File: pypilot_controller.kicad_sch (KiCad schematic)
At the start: 39 parts, among them J1 power+, J10 Clutch, J2 power-, J3 Motor A, J4 Motor B, Q1 Q_NMOS_GDS, Q2 Q_NMOS_GDS, Q3 Q_NMOS_GDS, Q4 Q_NMOS_GDS, Q5 Q_NMOS_GDS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

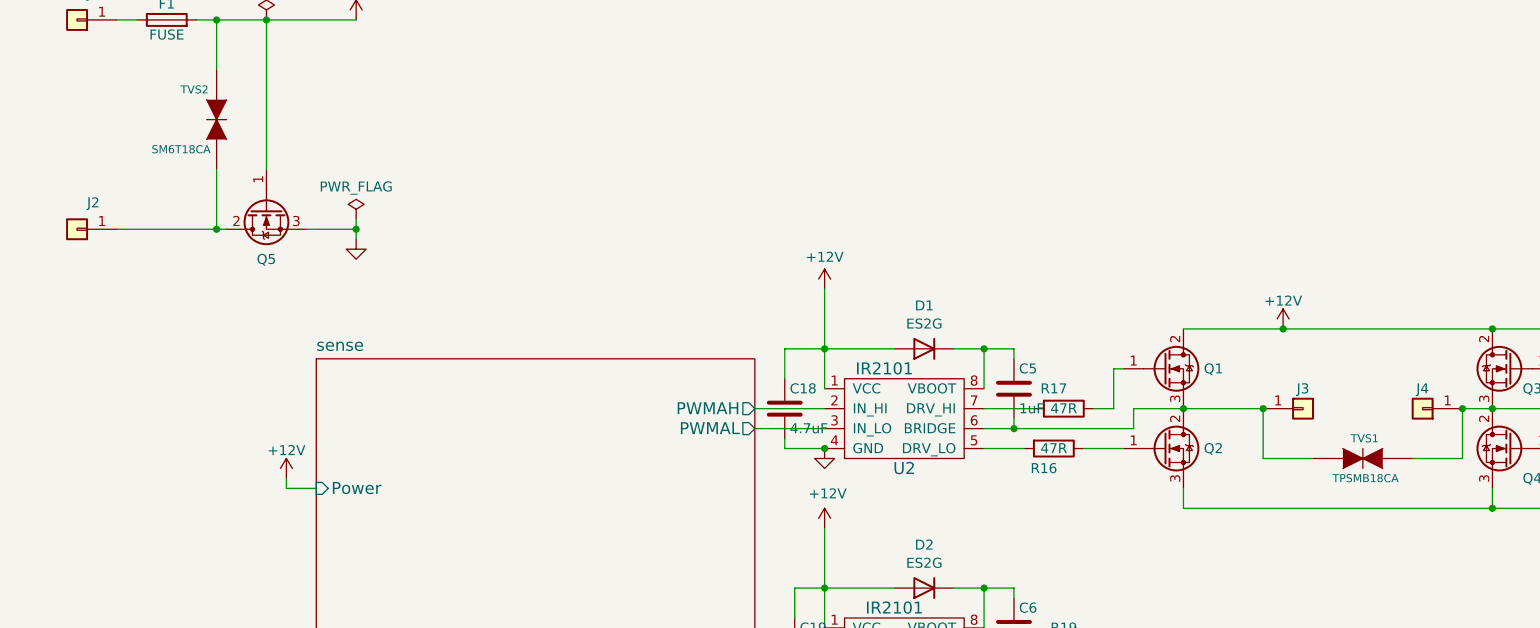
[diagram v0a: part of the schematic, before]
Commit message: Update TVS diodes to be cheapest of all the options Sean mentioned
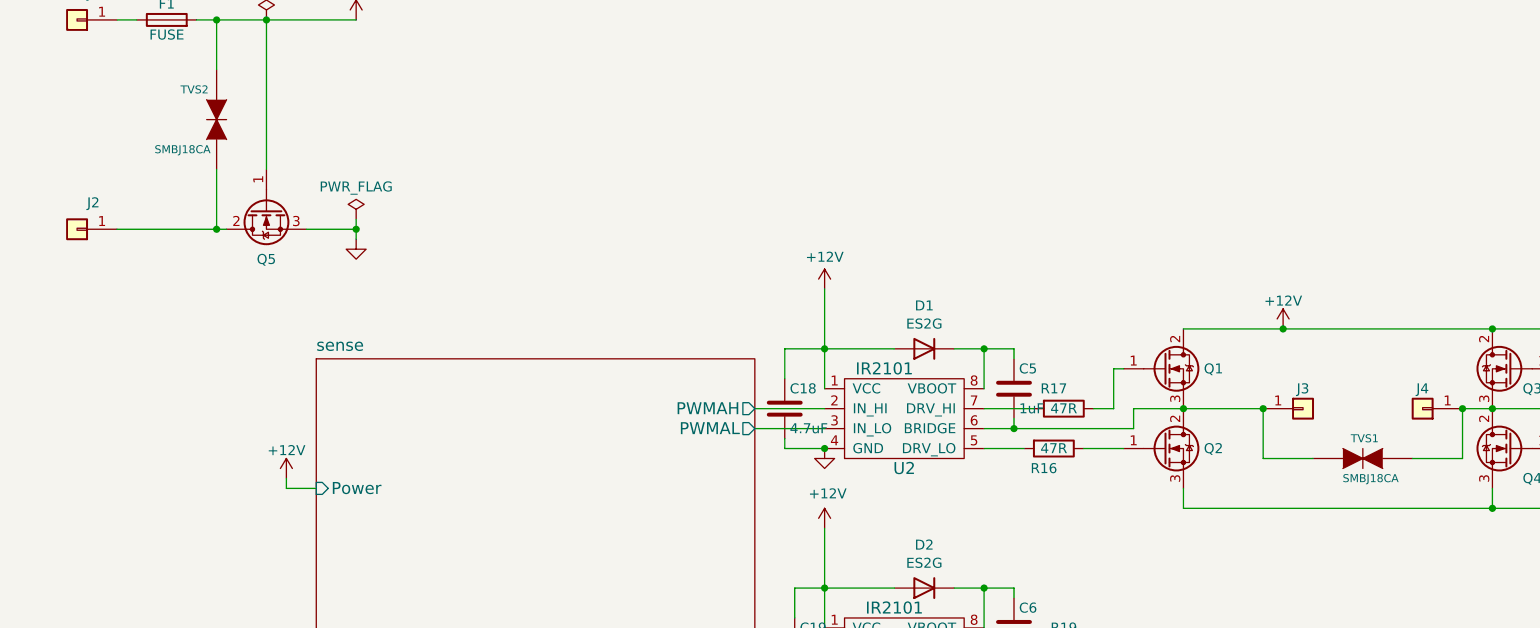
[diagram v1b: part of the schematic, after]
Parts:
- TVS1: value TPSMB18CA -> SMBJ18CA; LCSC *C83327, C468907 -> C83327
- TVS2: value SM6T18CA -> SMBJ18CA; LCSC *C83327, C283478 -> C83327
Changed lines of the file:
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@@
 			)
 		)
-		(property "Value" "TPSMB18CA"
+		(property "Value" "SMBJ18CA"
 			(at 201.422 88.9 0)
 			(effects
@@
 			)
 		)
-		(property "LCSC" "*C83327, C468907 "
+		(property "LCSC" "C83327"
 			(at 196.85 86.36 0)
 			(effects
@@
 			)
 		)
-		(property "Value" "SM6T18CA"
+		(property "Value" "SMBJ18CA"
 			(at 50.038 46.99 90)
 			(effects
@@
 			)
 		)
-		(property "LCSC" "*C83327, C283478"
+		(property "LCSC" "C83327"
 			(at 50.8 43.18 0)
 			(effects

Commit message: Updated screw terminals from C238164 to C481447, much cheaper
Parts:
- J1, J2, J3, J4: footprint pypilot_controller_footprints:screw_terminal -> lcsc:CONN-TH_T44001
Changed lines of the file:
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@@
 			)
 		)
-		(property "Footprint" "pypilot_controller_footprints:screw_terminal"
+		(property "Footprint" "lcsc:CONN-TH_T44001"
 			(at 33.02 57.15 0)
 			(effects
@@
 			)
 		)
-		(property "Footprint" "pypilot_controller_footprints:screw_terminal"
+		(property "Footprint" "lcsc:CONN-TH_T44001"
 			(at 33.02 30.48 0)
 			(effects
@@
 			)
 		)
-		(property "Footprint" "pypilot_controller_footprints:screw_terminal"
+		(property "Footprint" "lcsc:CONN-TH_T44001"
 			(at 189.23 80.01 0)
 			(effects
@@
 			)
 		)
-		(property "Footprint" "pypilot_controller_footprints:screw_terminal"
+		(property "Footprint" "lcsc:CONN-TH_T44001"
 			(at 204.47 80.01 0)
 			(effects

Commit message: Update 3d model and footprint for fuse holder
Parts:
- F1: footprint pypilot_controller_footprints:BladeFuse-CarType -> lcsc:FUSE-TH_BX503-35
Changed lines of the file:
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@@
 			)
 		)
-		(property "Footprint" "pypilot_controller_footprints:BladeFuse-CarType"
+		(property "Footprint" "lcsc:FUSE-TH_BX503-35"
 			(at 44.45 32.258 90)
 			(effects
@@
 			)
 		)
-		(property "Datasheet" "~"
+		(property "Datasheet" "https://www.lcsc.com/datasheet/lcsc_datasheet_2411201843_DEALON-BX503-35_C2935871.pdf"
 			(at 44.45 30.48 0)
 			(effects

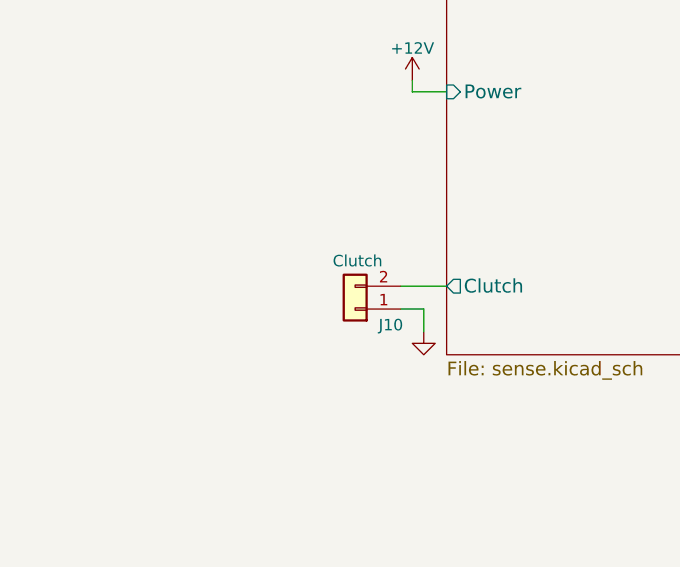
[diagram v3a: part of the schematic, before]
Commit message: Put clutch components onto separate sheet
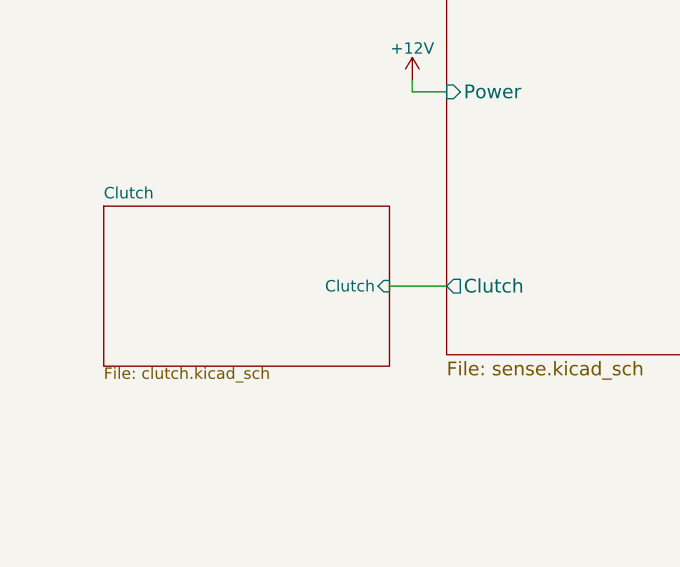
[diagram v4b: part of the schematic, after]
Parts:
- removed J10: Clutch, Connector_PinHeader_2.54mm:PinHeader_1x02_P2.54mm_Vertical, symbol Connector_Generic:Conn_01x02
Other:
- added sheet Clutch (clutch.kicad_sch)
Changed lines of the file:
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@@
 	(wire
 		(pts
-			(xy 58.42 114.3) (xy 60.96 114.3)
-		)
-		(stroke
-			(width 0)
-			(type default)
-		)
-	)
-	(wire
-		(pts
 			(xy 124.46 102.87) (xy 124.46 106.68)
 		)
@@
 	(wire
 		(pts
-			(xy 60.96 114.3) (xy 60.96 116.84)
-		)
-		(stroke
-			(width 0)
-			(type default)
-		)
-	)
-	(wire
-		(pts
 			(xy 165.1 80.01) (xy 165.1 74.93)
 		)
@@
 	(wire
 		(pts
+			(xy 57.15 111.76) (xy 63.5 111.76)
+		)
+		(stroke
+			(width 0)
+			(type default)
+		)
+	)
+	(wire
+		(pts
 			(xy 234.95 69.85) (xy 243.84 69.85)
 		)
@@
 	(wire
 		(pts
-			(xy 58.42 111.76) (xy 63.5 111.76)
-		)
-		(stroke
-			(width 0)
-			(type default)
-		)
-	)
-	(wire
-		(pts
 			(xy 128.27 85.09) (xy 123.19 85.09)
 		)
@@
 	)
 	(symbol
-		(lib_id "Connector_Generic:Conn_01x02")
-		(at 53.34 114.3 180)
-		(unit 1)
-		(exclude_from_sim no)
-		(in_bom yes)
-		(on_board yes)
-		(dnp no)
-		(property "Reference" "J10"
-			(at 58.674 116.078 0)
-			(effects
-				(font
-					(size 1.27 1.27)
-				)
-				(justify left)
-			)
-		)
-		(property "Value" "Clutch"
-			(at 56.388 108.966 0)
-			(effects
-				(font
-					(size 1.27 1.27)
-				)
-				(justify left)
-			)
-		)
-		(property "Footprint" "Connector_PinHeader_2.54mm:PinHeader_1x02_P2.54mm_Vertical"
-			(at 53.34 114.3 0)
-			(effects
-				(font
-					(size 1.27 1.27)
-				)
-				(hide yes)
-			)
-		)
-		(property "Datasheet" "~"
-			(at 53.34 114.3 0)
-			(effects
-				(font
-					(size 1.27 1.27)
-				)
-				(hide yes)
-			)
-		)
-		(property "Description" "Generic connector, single row, 01x02, script generated (kicad-library-utils/schlib/autogen/connector/)"
-			(at 53.34 114.3 0)
-			(effects
-				(font
-					(size 1.27 1.27)
-				)
-				(hide yes)
-			)
-		)
-		(pin "1"
-		)
-		(pin "2"
-		)
-		(instances
-			(project "pypilot_controller"
-				(path "/3485d22d-0932-4f13-a5db-09c3f9bc7038"
-					(reference "J10")
-					(unit 1)
-				)
-			)
-		)
-	)
-	(symbol
 		(lib_id "Mechanical:MountingHole")
 		(at 17.78 182.88 0)
@@
 	)
 	(symbol
-		(lib_id "power:GND")
-		(at 60.96 116.84 0)
-		(unit 1)
-		(exclude_from_sim no)
-		(in_bom yes)
-		(on_board yes)
-		(dnp no)
-		(property "Reference" "#PWR03"
-			(at 60.96 123.19 0)
-			(effects
-				(font
-					(size 1.27 1.27)
-				)
-				(hide yes)
-			)
-		)
-		(property "Value" "GND"
-			(at 57.15 118.11 0)
-			(effects
-				(font
-					(size 1.27 1.27)
-				)
-				(hide yes)
-			)
-		)
-		(property "Footprint" ""
-			(at 60.96 116.84 0)
-			(effects
-				(font
-					(size 1.27 1.27)
-				)
-				(hide yes)
-			)
-		)
-		(property "Datasheet" ""
-			(at 60.96 116.84 0)
-			(effects
-				(font
-					(size 1.27 1.27)
-				)
-				(hide yes)
-			)
-		)
-		(property "Description" "Power symbol creates a global label with name \"GND\" , ground"
-			(at 60.96 116.84 0)
-			(effects
-				(font
-					(size 1.27 1.27)
-				)
-				(hide yes)
-			)
-		)
-		(pin "1"
-		)
-		(instances
-			(project "pypilot_controller"
-				(path "/3485d22d-0932-4f13-a5db-09c3f9bc7038"
-					(reference "#PWR03")
-					(unit 1)
-				)
-			)
-		)
-	)
-	(symbol
 		(lib_id "power:PWR_FLAG")
 		(at 57.15 30.48 0)
@@
 				)
 			)
+		)
+	)
+	(sheet
+		(at 25.4 102.87)
+		(size 31.75 17.78)
+		(fields_autoplaced yes)
+		(stroke
+			(width 0.1524)
+			(type solid)
+			(color 132 0 132 1)
+		)
+		(fill
+			(color 255 255 255 0.0000)
+		)
+		(property "Sheetname" "Clutch"
+			(at 25.4 102.1584 0)
+			(effects
+				(font
+					(size 1.27 1.27)
+				)
+				(justify left bottom)
+			)
+		)
+		(property "Sheetfile" "clutch.kicad_sch"
+			(at 25.4 120.7266 0)
+			(effects
+				(font
+					(size 1.27 1.27)
+				)
+				(justify left top)
+			)
+		)
+		(pin "Clutch" input
+			(at 57.15 111.76 0)
+			(effects
+				(font
+					(size 1.27 1.27)
+				)
+				(justify right)
+			)
+		)
+		(instances
+			(project "pypilot_controller"
+				(path "/3485d22d-0932-4f13-a5db-09c3f9bc7038"
+					(page "4")
+				)
+			)

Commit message: Tweaks to hand-load components for current availability
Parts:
- J1, J2, J3, J4: LCSC C238164 -> C481447
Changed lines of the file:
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@@
 			)
 		)
-		(property "Datasheet" "~"
+		(property "Datasheet" "https://www.lcsc.com/datasheet/lcsc_datasheet_2304140030_BERYL-Electronic-Tech-RG063M331LO10-20TA-1A1E_C357629.pdf"
 			(at 229.87 80.01 0)
 			(effects
@@
 			)
 		)
-		(property "Datasheet" "~"
+		(property "Datasheet" "https://www.lcsc.com/datasheet/lcsc_datasheet_2304140030_BERYL-Electronic-Tech-RG063M331LO10-20TA-1A1E_C357629.pdf"
 			(at 234.95 86.36 0)
 			(effects
@@
 			)
 		)
-		(property "LCSC" "C238164"
+		(property "LCSC" "C481447"
 			(at 33.02 57.15 0)
 			(effects
@@
 			)
 		)
-		(property "LCSC" "C238164"
+		(property "LCSC" "C481447"
 			(at 33.02 30.48 0)
 			(effects
@@
 			)
 		)
-		(property "LCSC" "C238164"
+		(property "LCSC" "C481447"
 			(at 189.23 80.01 0)
 			(effects
@@
 			)
 		)
-		(property "LCSC" "C238164"
+		(property "LCSC" "C481447"
 			(at 204.47 80.01 0)
 			(effects

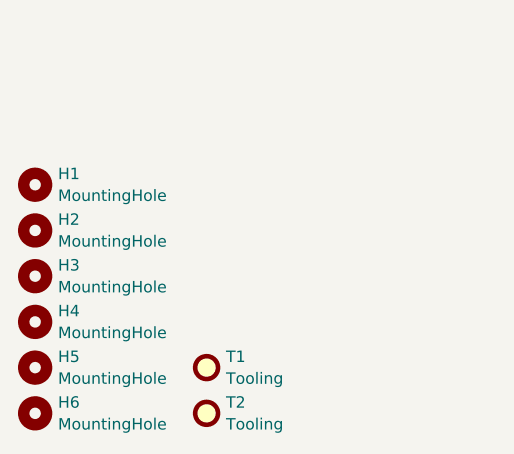
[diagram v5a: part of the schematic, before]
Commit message: Modify board outline to fit Daho 83X58X34 enclosure.  Remove mounting holes and move components.
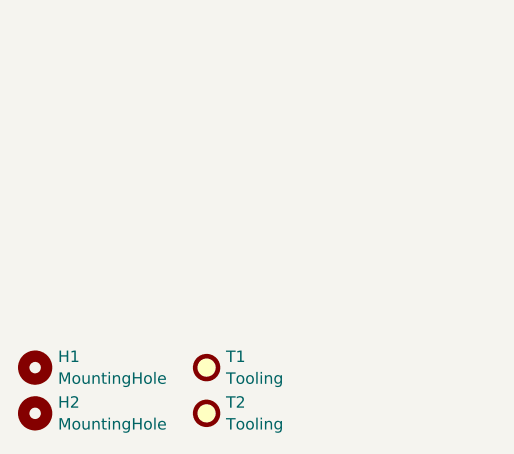
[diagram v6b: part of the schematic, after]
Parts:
- removed H1, H2, H3, H4: MountingHole, MountingHole:MountingHole_3.2mm_M3, symbol Mechanical:MountingHole
- renumbered H5 to H1, H6 to H2

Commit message: Added results of fit test to components received from LCSC
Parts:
- C10, C9: FitTest (none) -> ?
- D1, D2, J1, J2, J3, J4, Q1, Q2, Q3, Q4, Q5, R26, TVS1, TVS2, U2, U3: FitTest (none) -> Y
- F1: FitTest (none) -> N
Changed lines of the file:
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@@
+			)
+		)
+		(property "FitTest" "Y"
+			(at 215.9 85.09 0)
+			(effects
+				(font
+					(size 1.27 1.27)
+				)
+				(hide yes)
 			)
 		)
@@
 			)
 		)
+		(property "FitTest" "Y"
+			(at 138.43 73.66 0)
+			(effects
+				(font
+					(size 1.27 1.27)
+				)
+				(hide yes)
+			)
+		)
 		(pin "1"
 		)
@@
 		)
 		(property "LCSC" "C2956"
+			(at 138.43 104.14 0)
+			(effects
+				(font
+					(size 1.27 1.27)
+				)
+				(hide yes)
+			)
+		)
+		(property "FitTest" "Y"
 			(at 138.43 104.14 0)
 			(effects
@@
 			)
 		)
+		(property "FitTest" "Y"
+			(at 215.9 74.93 0)
+			(effects
+				(font
+					(size 1.27 1.27)
+				)
+				(hide yes)
+			)
+		)
 		(pin "2"
 		)
@@
 			)
 		)
+		(property "FitTest" "Y"
+			(at 171.45 74.93 0)
+			(effects
+				(font
+					(size 1.27 1.27)
+				)
+				(hide yes)
+			)
+		)
 		(pin "1"
 		)
@@
 			)
 		)
+		(property "FitTest" "Y"
+			(at 171.45 85.09 0)
+			(effects
+				(font
+					(size 1.27 1.27)
+				)
+				(hide yes)
+			)
+		)
 		(pin "2"
 		)
@@
 		)
 		(property "LCSC" "C83327"
+			(at 196.85 86.36 0)
+			(effects
+				(font
+					(size 1.27 1.27)
+				)
+				(hide yes)
+			)
+		)
+		(property "FitTest" "Y"
 			(at 196.85 86.36 0)
 			(effects
@@
 			)
 		)
+		(property "FitTest" "Y"
+			(at 57.15 54.61 0)
+			(effects
+				(font
+					(size 1.27 1.27)
+				)
+				(hide yes)
+			)
+		)
 		(pin "1"
 		)
@@
 			)
 		)
+		(property "FitTest" "?"
+			(at 229.87 80.01 0)
+			(effects
+				(font
+					(size 1.27 1.27)
+				)
+				(hide yes)
+			)
+		)
 		(pin "1"
 		)
@@
 			)
 		)
+		(property "FitTest" "?"
+			(at 234.95 86.36 0)
+			(effects
+				(font
+					(size 1.27 1.27)
+				)
+				(hide yes)
+			)
+		)
 		(pin "1"
 		)
@@
 			)
 		)
+		(property "FitTest" "Y"
+			(at 50.8 43.18 0)
+			(effects
+				(font
+					(size 1.27 1.27)
+				)
+				(hide yes)
+			)
+		)
 		(pin "1"
 		)
@@
 			)
 		)
+		(property "FitTest" "Y"
+			(at 140.97 72.39 0)
+			(effects
+				(font
+					(size 1.27 1.27)
+				)
+				(hide yes)
+			)
+		)
 		(pin "1"
 		)
@@
 			)
 		)
+		(property "FitTest" "Y"
+			(at 140.97 102.87 0)
+			(effects
+				(font
+					(size 1.27 1.27)
+				)
+				(hide yes)
+			)
+		)
 		(pin "1"
 		)
@@
 			)
 		)
+		(property "FitTest" "N"
+			(at 44.45 30.48 0)
+			(effects
+				(font
+					(size 1.27 1.27)
+				)
+				(hide yes)
+			)
+		)
 		(pin "1"
 		)
@@
 			)
 		)
+		(property "FitTest" "Y"
+			(at 33.02 57.15 0)
+			(effects
+				(font
+					(size 1.27 1.27)
+				)
+				(hide yes)
+			)
+		)
 		(pin "1"
 		)
@@
 			)
 		)
+		(property "FitTest" "Y"
+			(at 33.02 30.48 0)
+			(effects
+				(font
+					(size 1.27 1.27)
+				)
+				(hide yes)
+			)
+		)
 		(pin "1"
 		)
@@
 			)
 		)
+		(property "FitTest" "Y"
+			(at 189.23 80.01 0)
+			(effects
+				(font
+					(size 1.27 1.27)
+				)
+				(hide yes)
+			)
+		)
 		(pin "1"
 		)
@@
 		)
 		(property "LCSC" "C481447"
+			(at 204.47 80.01 0)
+			(effects
+				(font
+					(size 1.27 1.27)
+				)
+				(hide yes)
+			)
+		)
+		(property "FitTest" "Y"
 			(at 204.47 80.01 0)
 			(effects
@@
 			(effects
 				(font
+					(size 1.27 1.27)
+				)
+				(hide yes)
+			)
+		)
+		(property "FitTest" "Y"
+			(at 245.11 101.6 0)
+			(effects
+				(font

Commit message: Specify MOSFET
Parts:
- Q1, Q2, Q3, Q4, Q5: value Q_NMOS_GDS -> IRFR7440
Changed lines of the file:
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@@
 			)
 		)
-		(property "Value" "Q_NMOS_GDS"
+		(property "Value" "IRFR7440"
 			(at 209.5246 85.09 90)
 			(effects
@@
 			)
 		)
-		(property "Value" "Q_NMOS_GDS"
+		(property "Value" "IRFR7440"
 			(at 209.5246 74.93 90)
 			(effects
@@
 			)
 		)
-		(property "Value" "Q_NMOS_GDS"
+		(property "Value" "IRFR7440"
 			(at 177.8254 74.93 90)
 			(effects
@@
 			)
 		)
-		(property "Value" "Q_NMOS_GDS"
+		(property "Value" "IRFR7440"
 			(at 177.8254 85.09 90)
 			(effects
@@
 			)
 		)
-		(property "Value" "Q_NMOS_GDS"
+		(property "Value" "IRFR7440"
 			(at 57.15 60.9854 90)
 			(effects
